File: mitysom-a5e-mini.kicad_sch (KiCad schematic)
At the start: 23 parts, among them J201 Plug_Samtec_SEAM-50-02.0-L-08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, J202 PinHeader_1x3_P2.54mm_Drill1.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

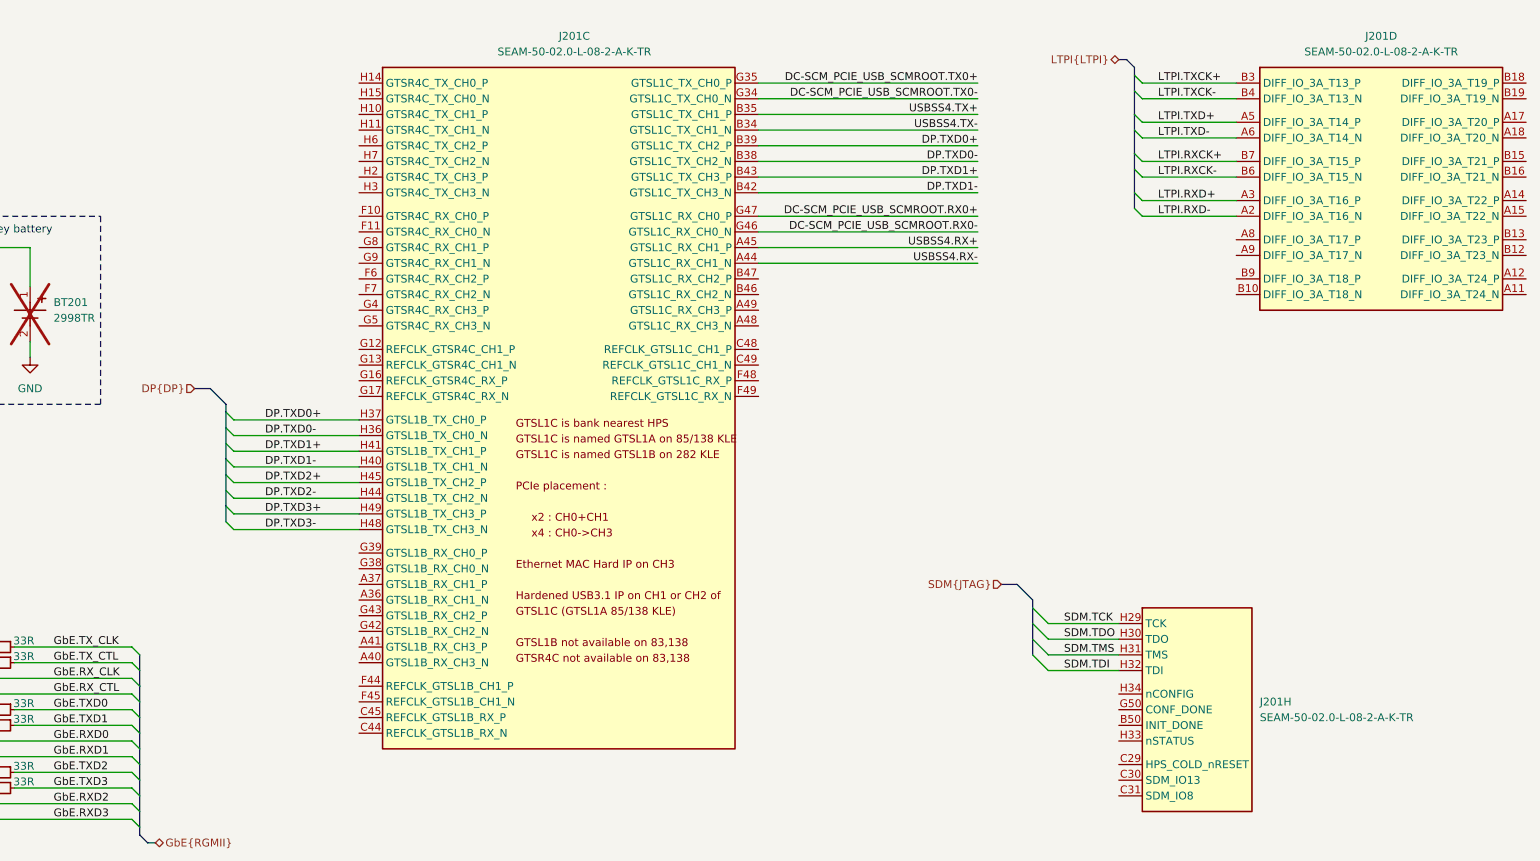
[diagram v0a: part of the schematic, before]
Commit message: [#99754] Improve LTPI to MitySOM-A5E connection
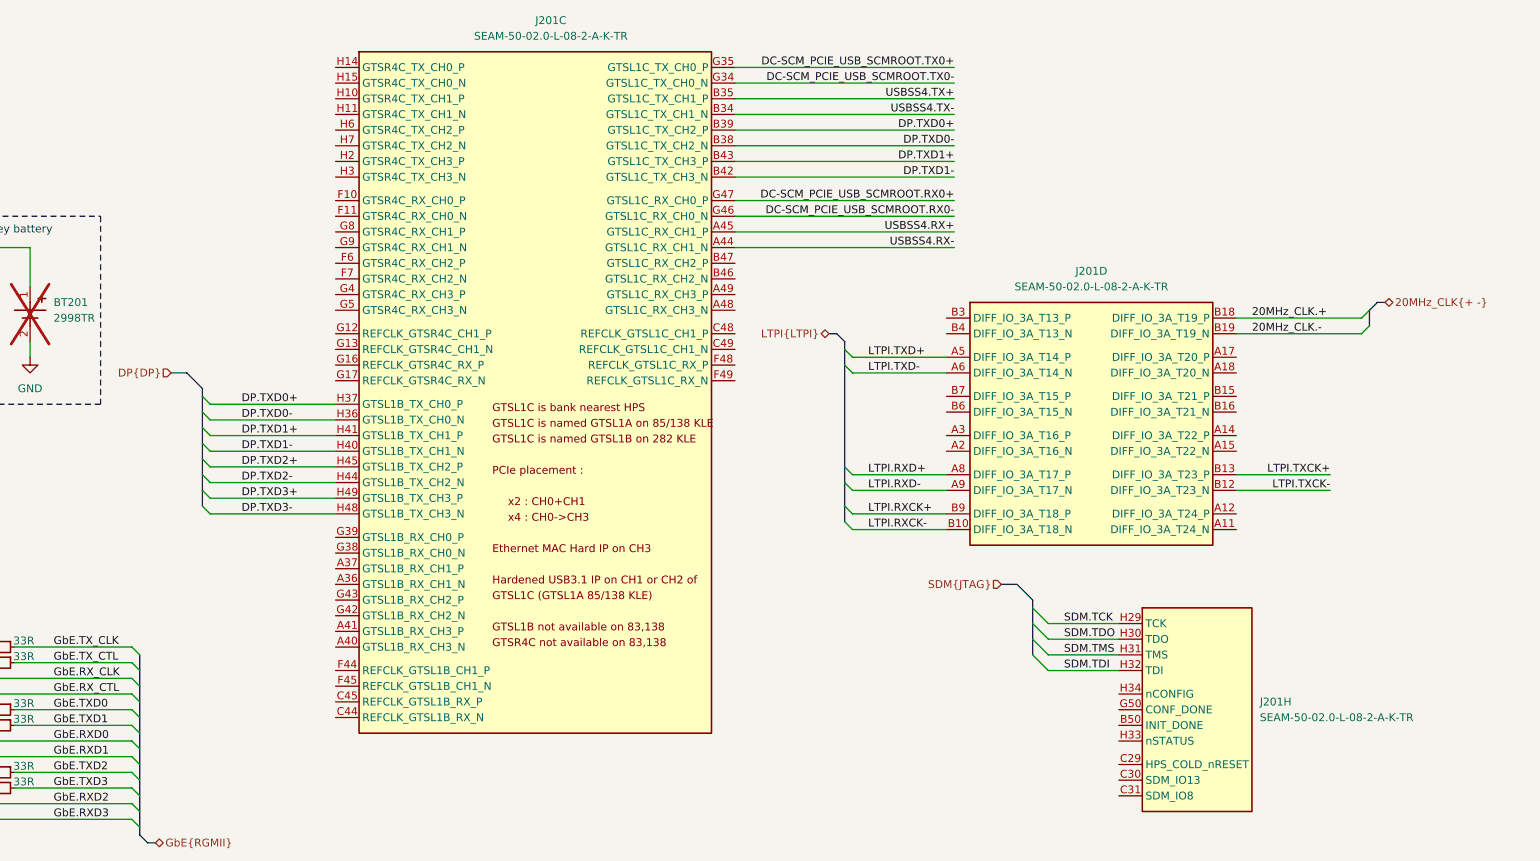
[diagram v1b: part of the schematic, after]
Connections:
- net LTPI.RXCK+: now also J201.B9 (DIFF_IO_3A_T18_P); no longer J201.B7 (DIFF_IO_3A_T15_P)
- net LTPI.RXCK-: now also J201.B10 (DIFF_IO_3A_T18_N); no longer J201.B6 (DIFF_IO_3A_T15_N)
- net LTPI.RXD+: now also J201.A8 (DIFF_IO_3A_T17_P); no longer J201.A3 (DIFF_IO_3A_T16_P)
- net LTPI.RXD-: now also J201.A9 (DIFF_IO_3A_T17_N); no longer J201.A2 (DIFF_IO_3A_T16_N)
- net LTPI.TXCK+: now also J201.B13 (DIFF_IO_3A_T23_P); no longer J201.B3 (DIFF_IO_3A_T13_P)
- net LTPI.TXCK-: now also J201.B12 (DIFF_IO_3A_T23_N); no longer J201.B4 (DIFF_IO_3A_T13_N)
- net 20MHz_CLK.+: now reaches J201.B18 (DIFF_IO_3A_T19_P)
- net 20MHz_CLK.-: now reaches J201.B19 (DIFF_IO_3A_T19_N)
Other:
- moved on the sheet: J201C, J201D

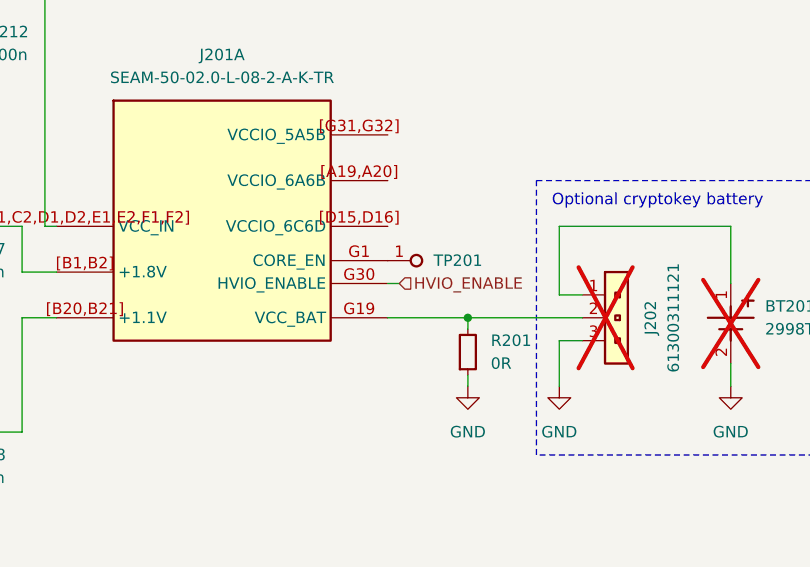
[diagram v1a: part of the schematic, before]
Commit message: [#99974] Connect remaining DC-SCM signals on root schematic, except for I2C
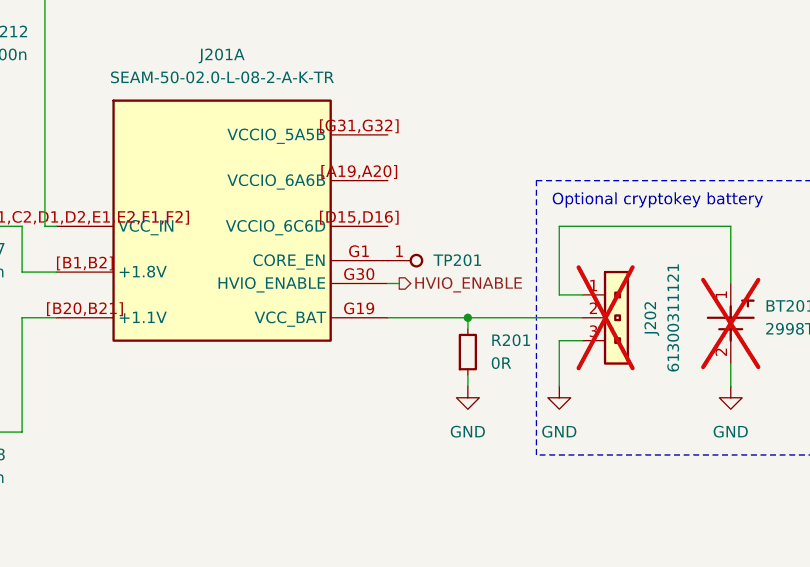
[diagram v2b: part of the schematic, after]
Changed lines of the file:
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@@
 	)
 	(hierarchical_label "HVIO_ENABLE"
-		(shape input)
+		(shape output)
 		(at 132.08 67.31 0)
 		(effects
@@
 			(justify left bottom)
 		)
-		(property "Netclass" "100Ohm-diff"
+		(property "Net Class" "100Ohm-diff"
 			(at 193.548 102.87 0)
 			(show_name no)
@@
 			(justify left bottom)
 		)
-		(property "Netclass" "100Ohm-diff"
+		(property "Net Class" "100Ohm-diff"
 			(at 297.688 78.74 0)
 			(show_name no)
@@
 			(justify right bottom)
 		)
-		(property "Netclass" "100Ohm-diff"
+		(property "Net Class" "100Ohm-diff"
 			(at 261.112 238.76 0)
 			(show_name no)

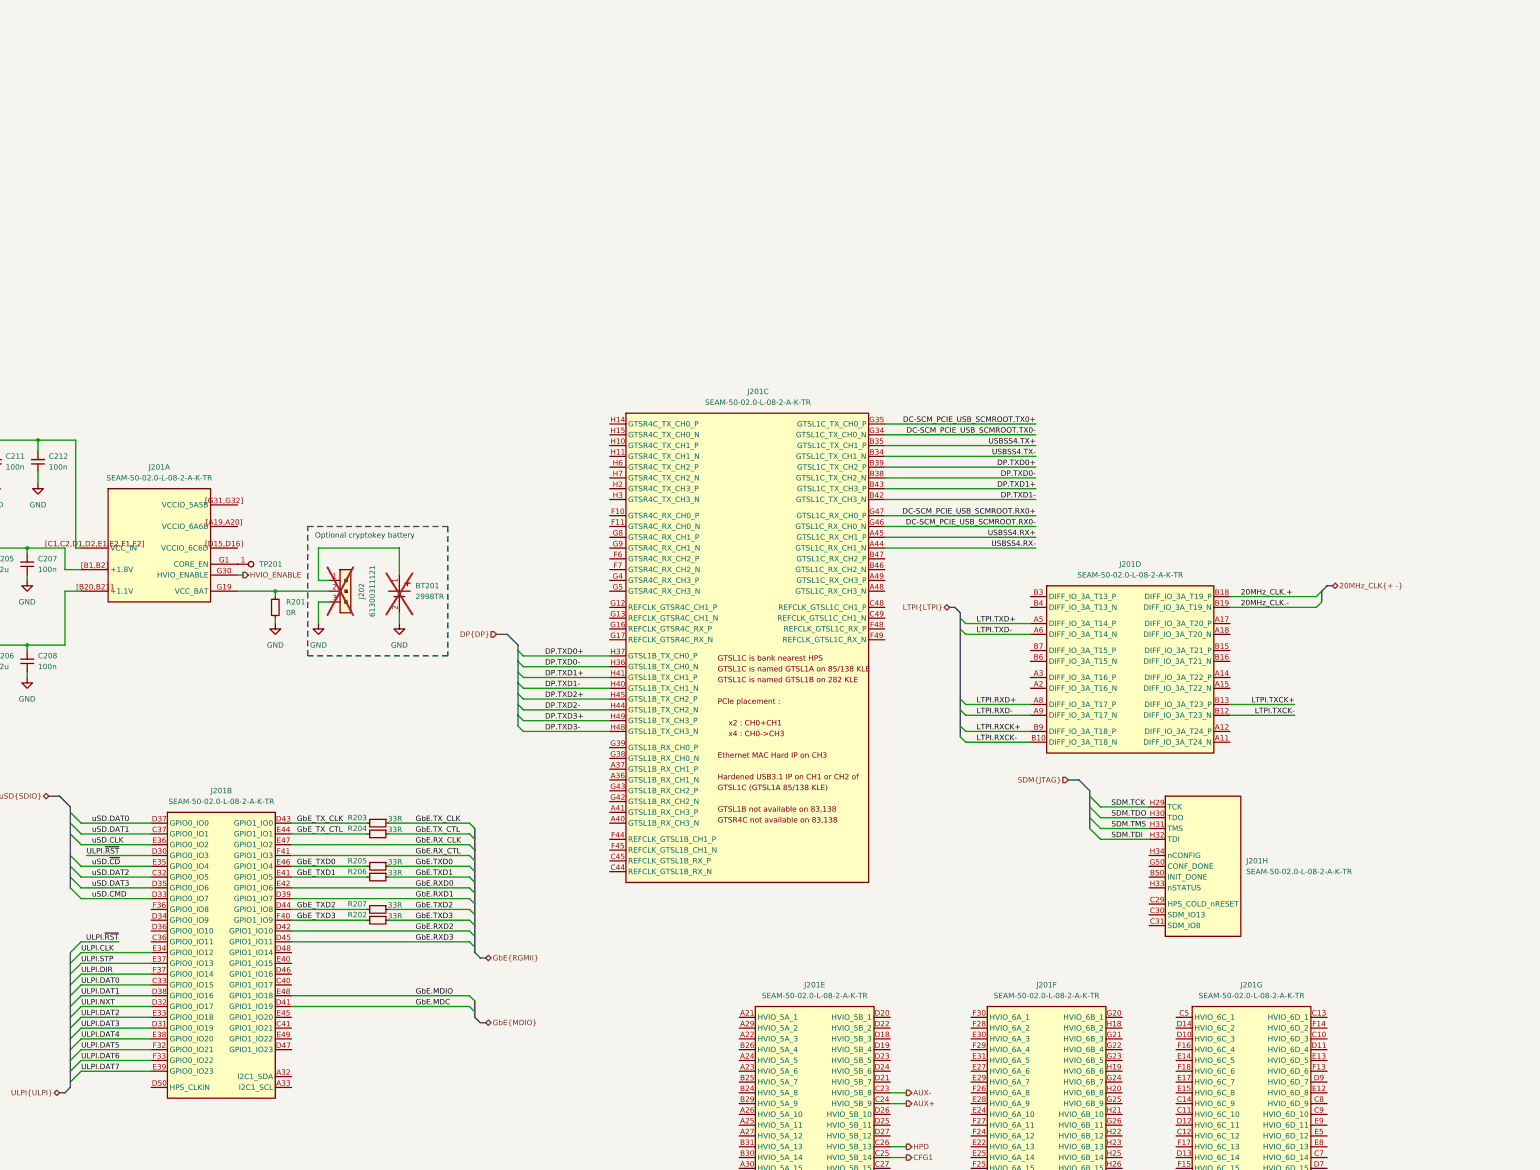
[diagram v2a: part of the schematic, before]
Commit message: [#100060] Add and connect high speed connector
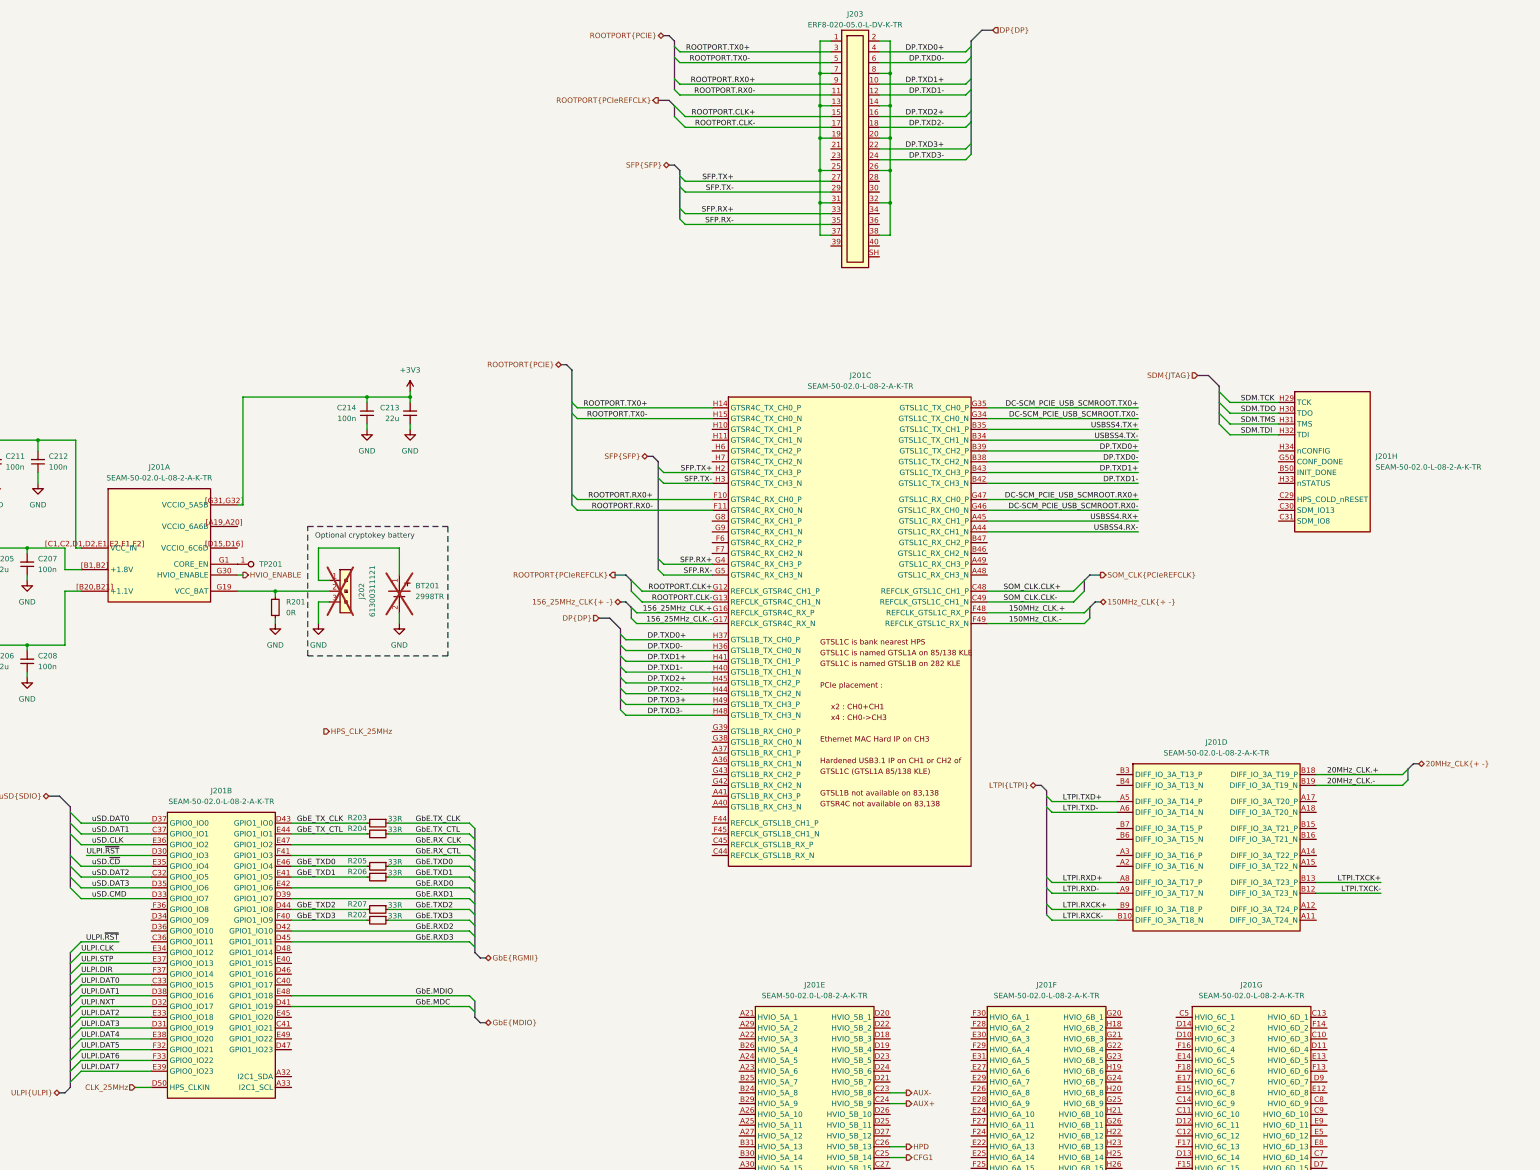
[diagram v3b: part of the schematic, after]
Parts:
- added C213: C_22u_10V_0402, antmicro-footprints:C_0402_1005Metric, symbol antmicroCapacitors0402:C_22u_10V_0402
- added C214: C_100n_0402, antmicro-footprints:C_0402_1005Metric, symbol antmicroCapacitors0402:C_100n_0402
- added J203: Socket_Samtec_ERF8_2x20_ERF8-020-05.0-L-DV-K-TR, antmicro-footprints:Conn_Socket_Samtec_ERF8_2x20_ERF8-020-05.0-L-DV-K-TR, symbol antmicroB2BConnectors:Socket_Samtec_ERF8_2x20_ERF8-020-05.0-L-DV-K-TR
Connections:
- net DP.TXD0+: now also J203.4
- net DP.TXD0-: now also J203.6
- net DP.TXD1+: now also J203.10
- net DP.TXD1-: now also J203.12
- net DP.TXD2+: now also J203.16
- net DP.TXD2-: now also J203.18
- net DP.TXD3+: now also J203.22
- net DP.TXD3-: now also J203.24
- net GND: now also C213.1, C214.1
- net +3V3: now reaches J201.[G31,G32] (VCCIO_5A5B)
- net +3V3: now also C213.2, C214.2
- net CLK_25MHz: now reaches J201.D50 (HPS_CLKIN)
- net SOM_CLK.CLK+: now reaches J201.C48 (REFCLK_GTSL1C_CH1_P)
- net SOM_CLK.CLK-: now reaches J201.C49 (REFCLK_GTSL1C_CH1_N)
- net ROOTPORT.RX0+: now reaches J201.F10 (GTSR4C_RX_CH0_P)
- net ROOTPORT.RX0+: now also J203.9
- net ROOTPORT.RX0-: now reaches J201.F11 (GTSR4C_RX_CH0_N)
- net ROOTPORT.RX0-: now also J203.11
- net 150MHz_CLK.+: now reaches J201.F48 (REFCLK_GTSL1C_RX_P)
- net 150MHz_CLK.-: now reaches J201.F49 (REFCLK_GTSL1C_RX_N)
- net ROOTPORT.CLK+: now reaches J201.G12 (REFCLK_GTSR4C_CH1_P)
- net ROOTPORT.CLK+: now also J203.15
- net ROOTPORT.CLK-: now reaches J201.G13 (REFCLK_GTSR4C_CH1_N)
- net ROOTPORT.CLK-: now also J203.17
- net 156_25MHz_CLK.+: now reaches J201.G16 (REFCLK_GTSR4C_RX_P)
- net 156_25MHz_CLK.-: now reaches J201.G17 (REFCLK_GTSR4C_RX_N)
- net SFP.RX+: now reaches J201.G4 (GTSR4C_RX_CH3_P)
- net SFP.RX+: now also J203.33
- net SFP.RX-: now reaches J201.G5 (GTSR4C_RX_CH3_N)
- net SFP.RX-: now also J203.35
- net ROOTPORT.TX0+: now reaches J201.H14 (GTSR4C_TX_CH0_P)
- net ROOTPORT.TX0+: now also J203.3
- net ROOTPORT.TX0-: now reaches J201.H15 (GTSR4C_TX_CH0_N)
- net ROOTPORT.TX0-: now also J203.5
- net SFP.TX+: now reaches J201.H2 (GTSR4C_TX_CH3_P)
- net SFP.TX+: now also J203.27
- net SFP.TX-: now reaches J201.H3 (GTSR4C_TX_CH3_N)
- net SFP.TX-: now also J203.29
- new net: J203.1, J203.13, J203.19, J203.25, J203.31, J203.37, J203.7
- new net: J203.14, J203.2, J203.20, J203.26, J203.32, J203.38, J203.8
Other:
- moved on the sheet: J201C, J201D, J201H
